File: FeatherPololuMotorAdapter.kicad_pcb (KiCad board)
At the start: 2 copper layers, 2 parts, among them P1 CONN_01X04, P2 CONN_02X08

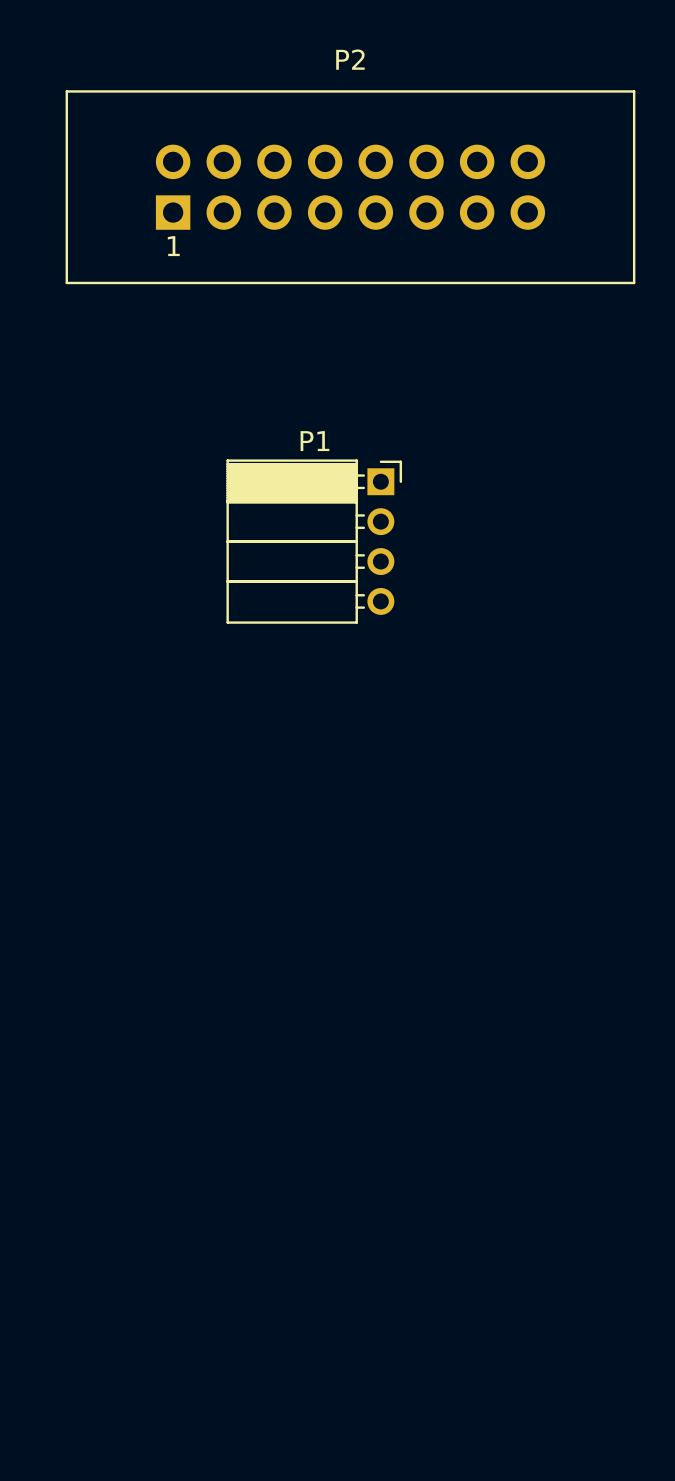
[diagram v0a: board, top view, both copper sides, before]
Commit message: Finished schematic. Started work on layout.
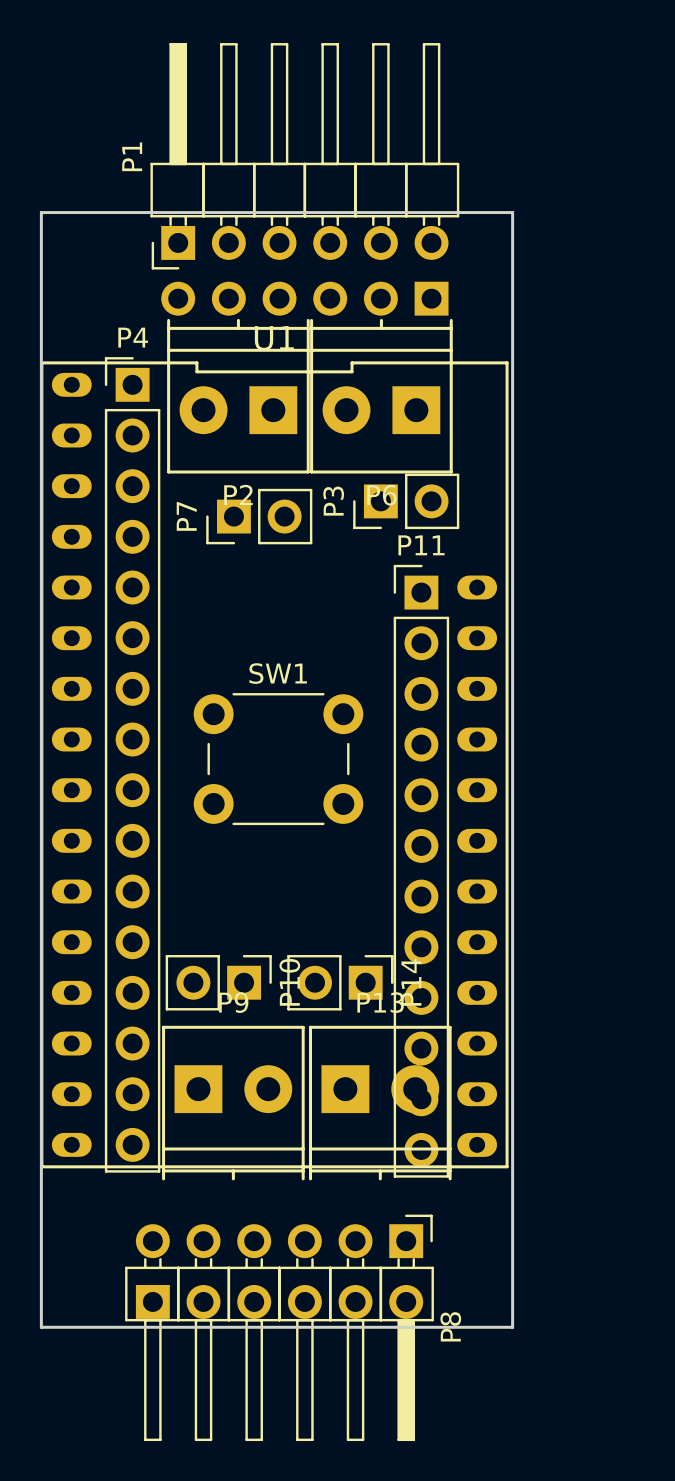
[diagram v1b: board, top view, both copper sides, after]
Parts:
- added P10: ENC3_JMP, Pin_Headers:Pin_Header_Straight_1x02_Pitch2.54mm, F.Cu at (27.9, 61.5)
- added P11: CONN_01X12, Pin_Headers:Pin_Header_Straight_1x12_Pitch2.54mm, F.Cu at (36.8, 41.9)
- added P12: MOTOR4, Pin_Headers:Pin_Header_Angled_1x06_Pitch2.54mm, B.Cu at (23.4, 77.5)
- added P13: MOTOR4_PWR, Terminal_Blocks:TerminalBlock_Pheonix_PT-3.5mm_2pol, F.Cu at (33.0, 66.8)
- added P14: ENC4_JMP, Pin_Headers:Pin_Header_Straight_1x02_Pitch2.54mm, F.Cu at (34.0, 61.5)
- added P3: ENC1_JMP, Pin_Headers:Pin_Header_Straight_1x02_Pitch2.54mm, F.Cu at (34.8, 37.3)
- added P4: CONN_01X16, Pin_Headers:Pin_Header_Straight_1x16_Pitch2.54mm, F.Cu at (22.4, 31.5)
- added P5: MOTOR2, Pin_Headers:Pin_Header_Angled_1x06_Pitch2.54mm, B.Cu at (37.3, 27.2)
- added P6: MOTOR2_PWR, Terminal_Blocks:TerminalBlock_Pheonix_PT-3.5mm_2pol, F.Cu at (36.6, 32.8)
- added P7: ENC2_JMP, Pin_Headers:Pin_Header_Straight_1x02_Pitch2.54mm, F.Cu at (27.4, 38.1)
- added P8: MOTOR3, Pin_Headers:Pin_Header_Angled_1x06_Pitch2.54mm, F.Cu at (36.1, 74.4)
- added P9: MOTOR3_PWR, Terminal_Blocks:TerminalBlock_Pheonix_PT-3.5mm_2pol, F.Cu at (25.7, 66.8)
- added SW1: RESET, Buttons_Switches_ThroughHole:SW_PUSH_6mm, F.Cu at (26.4, 48.0)
- added U1: GenericFeather, schminktronics:Adafruit_Feather, F.Cu at (29.5, 50.5)
- P1: value CONN_01X04 -> MOTOR1; footprint Socket_Strips:Socket_Strip_Angled_1x04_Pitch2.00mm -> Pin_Headers:Pin_Header_Angled_1x06_Pitch2.54mm
- P2: value CONN_02X08 -> MOTOR1_PWR; footprint Connect:IDC_Header_Straight_16pins -> Terminal_Blocks:TerminalBlock_Pheonix_PT-3.5mm_2pol
- moved P1 15.7 mm to (24.6, 24.4), turned to 90 degrees
- moved P2 11.1 mm to (29.4, 32.8), turned to 180 degrees
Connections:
- P1 pad 1: Net-(P1-Pad1) -> M1_V+
- P1 pad 2: Net-(P1-Pad2) -> M1_V-
- P1 pad 3: Net-(P1-Pad3) -> ENC_GND
- P1 pad 4: Net-(P1-Pad4) -> ENC_VCC
- P2 pad 1: Net-(P2-Pad1) -> M1_V+
- P2 pad 2: Net-(P2-Pad2) -> M1_V-
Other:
- board outline added: 23.6 x 55.9 mm

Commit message: Finished schematic and layout.
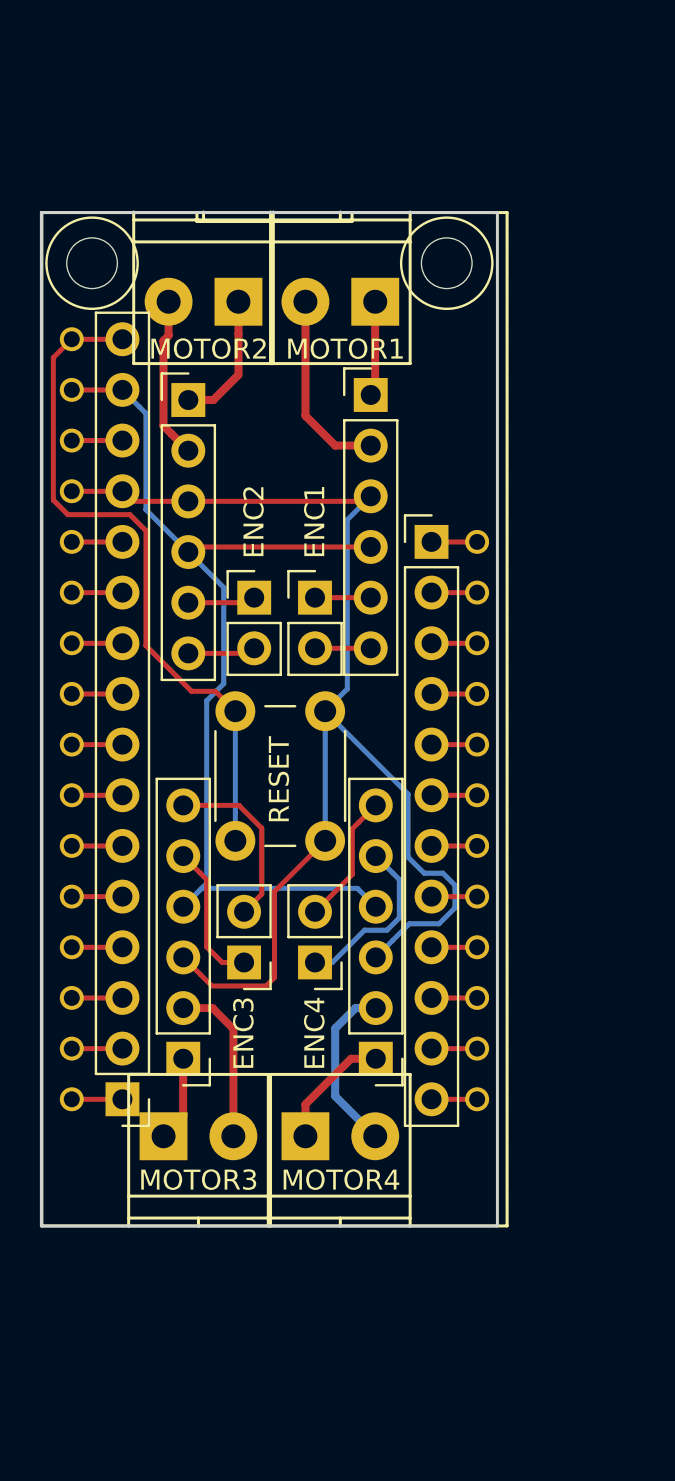
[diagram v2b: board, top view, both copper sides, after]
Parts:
- added REF**: 1pin, Connect:1pin, F.Cu at (38.1, 25.4)
- added REF**: 1pin, Connect:1pin, F.Cu at (20.3, 25.4)
- P1, P8: footprint Pin_Headers:Pin_Header_Angled_1x06_Pitch2.54mm -> Pin_Headers:Pin_Header_Straight_1x06_Pitch2.54mm
- P10: value ENC3_JMP -> ENC3
- P12, P5: footprint Pin_Headers:Pin_Header_Angled_1x06_Pitch2.54mm -> Pin_Headers:Pin_Header_Straight_1x06_Pitch2.54mm; moved to F.Cu
- P13: value MOTOR4_PWR -> MOTOR4
- P14: value ENC4_JMP -> ENC4
- P2: value MOTOR1_PWR -> MOTOR1
- P3: value ENC1_JMP -> ENC1
- P6: value MOTOR2_PWR -> MOTOR2
- P7: value ENC2_JMP -> ENC2
- P9: value MOTOR3_PWR -> MOTOR3
- moved P4 35.8 mm to (21.8, 67.3), turned to 180 degrees
- moved P12 16.5 mm to (34.5, 65.3), turned to 180 degrees
- moved P8 14.4 mm to (24.9, 65.3), turned to 180 degrees
- moved P5 13.2 mm to (25.1, 32.3), turned to 0 degrees
- moved P1 12.3 mm to (34.3, 32.0), turned to 0 degrees
- moved P6 10.4 mm to (27.7, 27.3)
- moved P2 7.46 mm to (34.5, 27.3)
- moved SW1 6.44 mm to (27.5, 54.4), turned to 90 degrees
- moved P3 5.85 mm to (31.5, 42.2), turned to 0 degrees
- moved P7 4.19 mm to (28.4, 42.2), turned to 0 degrees
- moved P13 3.10 mm to (31.0, 69.2)
- moved P9 2.94 mm to (23.9, 69.2)
- moved P14 2.74 mm to (31.5, 60.5), turned to 180 degrees
- moved P11 2.59 mm to (37.3, 39.4)
- moved U1 2.29 mm to (29.5, 48.3)
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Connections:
- P4 pad 13: GND -> ENC_GND
- P4 pad 15: Net-(P4-Pad15) -> ENC_VCC
- SW1 pad 2: GND -> ENC_GND
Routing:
- net ENC_GND: track 0.00 -> 64.9 mm
- net ENC_VCC: track 0.00 -> 51.1 mm
- net /RESET: track 0.00 -> 34.4 mm
- net M1_V-: track 0.00 -> 9.61 mm
- net ENC3_B: track 0.00 -> 8.97 mm
- net ENC4_A: track 0.00 -> 8.74 mm
- net M4_V-: track 0.00 -> 8.69 mm
- net M3_V-: track 0.00 -> 8.33 mm
- net M2_V-: track 0.00 -> 8.09 mm
- net ENC3_A: track 0.00 -> 7.24 mm
- net M2_V+: track 0.00 -> 6.70 mm
- net ENC4_B: track 0.00 -> 6.60 mm
- net M4_V+: track 0.00 -> 6.07 mm
- net M1_V+: track 0.00 -> 4.77 mm
- net M3_V+: track 0.00 -> 4.30 mm
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- added copper zone on B.Cu, net ENC_GND
- added copper zone on F.Cu, net ENC_GND
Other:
- board size 23.6 x 55.9 mm -> 22.9 x 50.8 mm
- net class Power added: clearance 0.2, trace_width 0.4, via_dia 0.6, via_drill 0.4
- board text added: "Feather Pololu"
- board text added: "May 18, 2017"
- board text added: "Motor Adapter"
- board text added: "V1"
